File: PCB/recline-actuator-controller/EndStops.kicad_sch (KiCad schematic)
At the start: 0 parts

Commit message: Recline Actuator Control
Recline controller board schematic and Recline actuator board schematics. Actuator control board schematic 90% complete.
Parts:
- added J12, J13, J14, J15: 0705530002, AVR-KiCAD-Lib-Connectors:Pin_Header_Angled_1x03_Pitch2.54mm, symbol AVR-KiCAD-Lib-Connectors:0705530002
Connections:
- new net +3.3V: J12.3, J13.3, J14.3, J15.3
- new net GND: J12.2, J13.2, J14.2, J15.2
- new net MAX1: J12.1
- new net MAX2: J14.1
- new net MIN1: J13.1
- new net MIN2: J15.1
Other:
- note added: "Endstops"

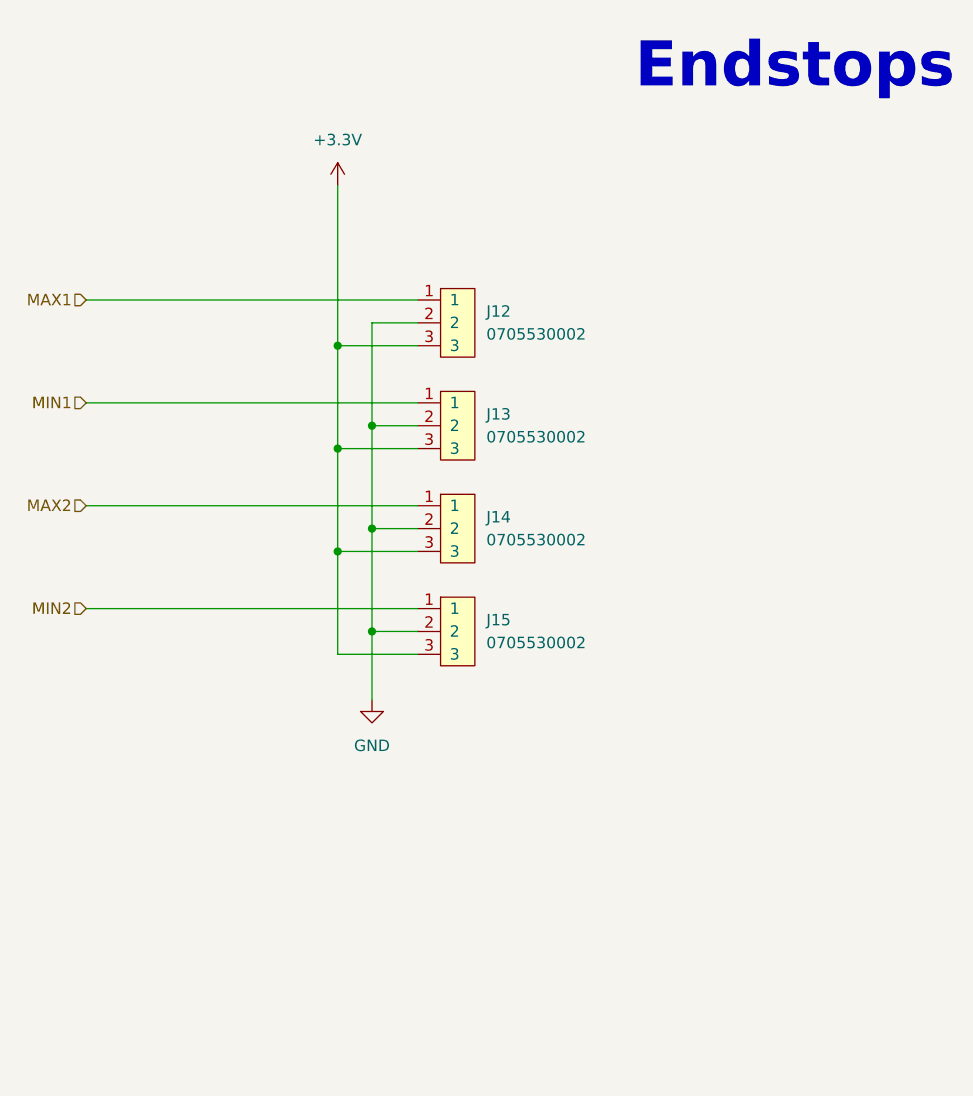
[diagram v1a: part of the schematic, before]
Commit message: Actuator Control Schematic
Schematic for Actuator control board completed! Once reviewed PCB layout will start.
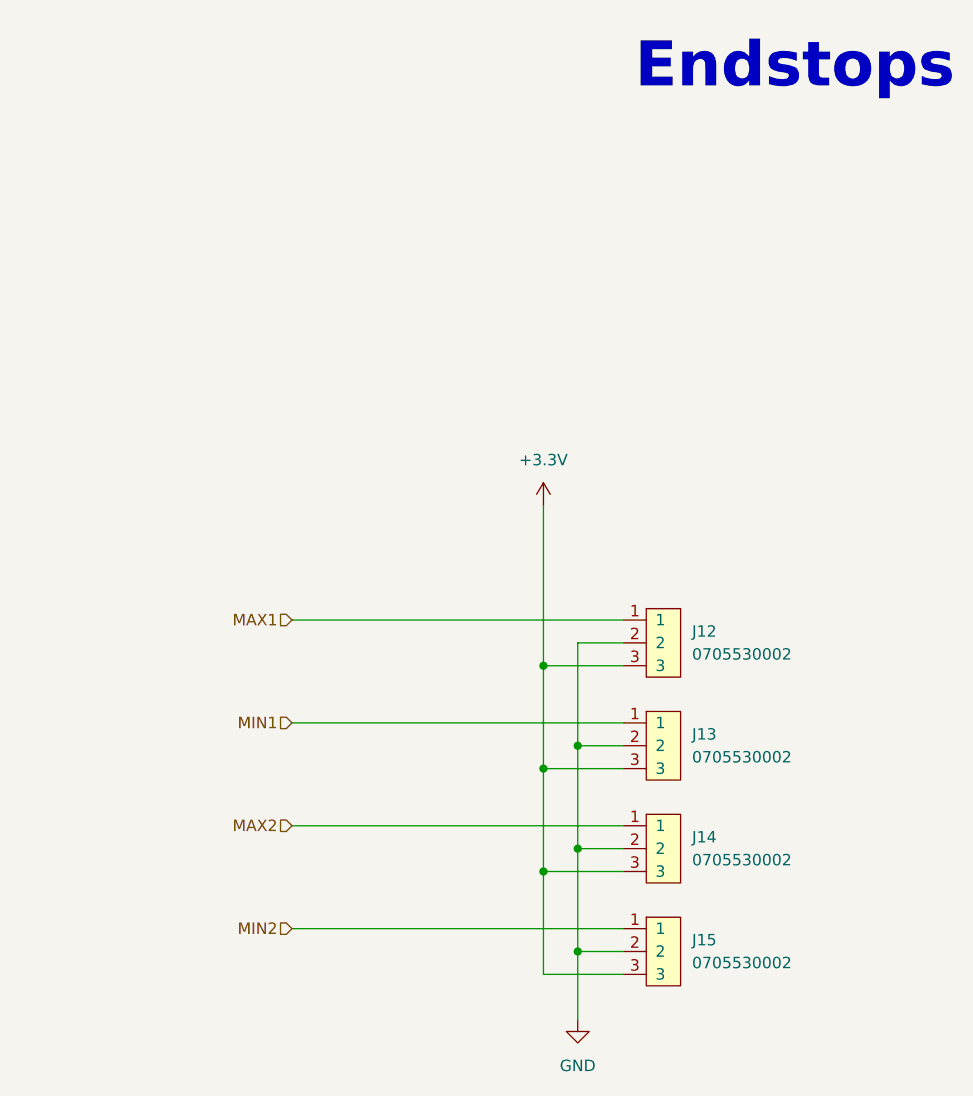
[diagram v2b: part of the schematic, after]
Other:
- moved on the sheet: J12, J13, J14, J15

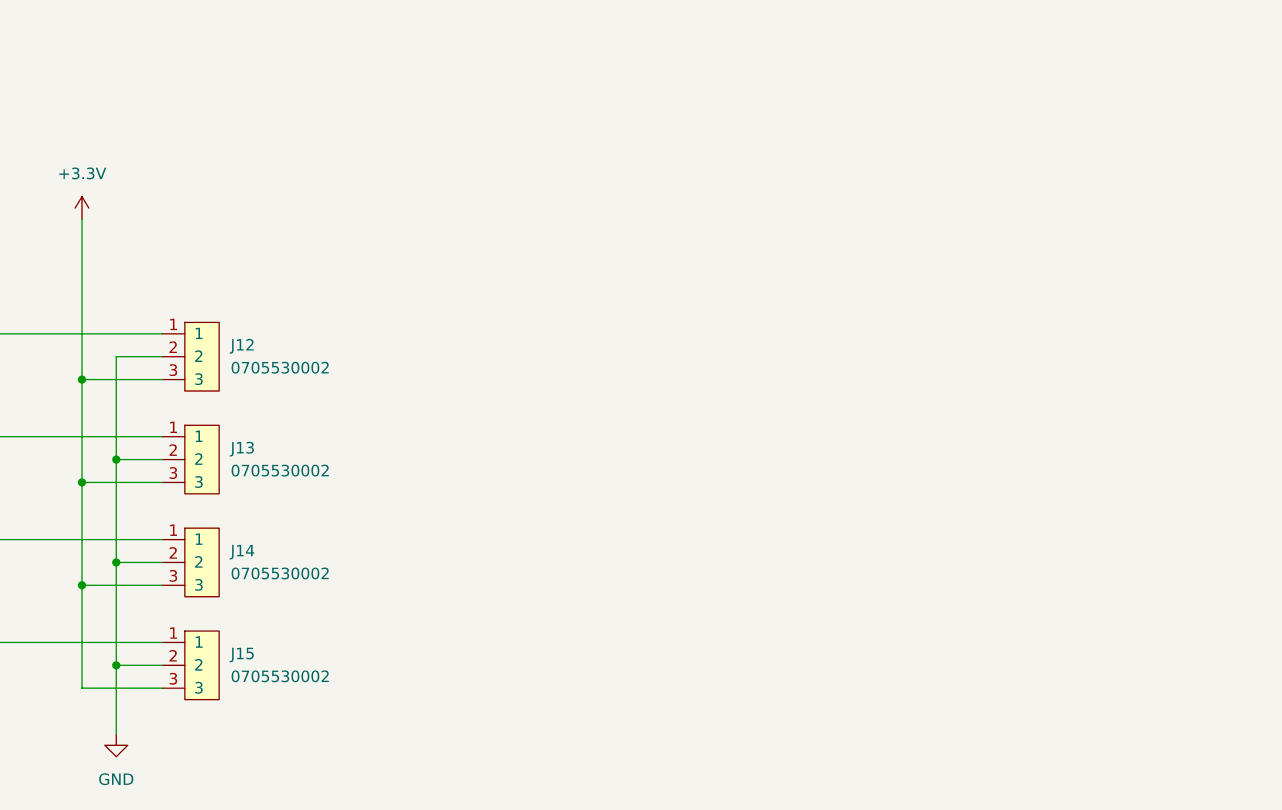
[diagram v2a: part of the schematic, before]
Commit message: More Motor Channels
Adding more motor channels to actuator control board it will need new MCU or port expansion.
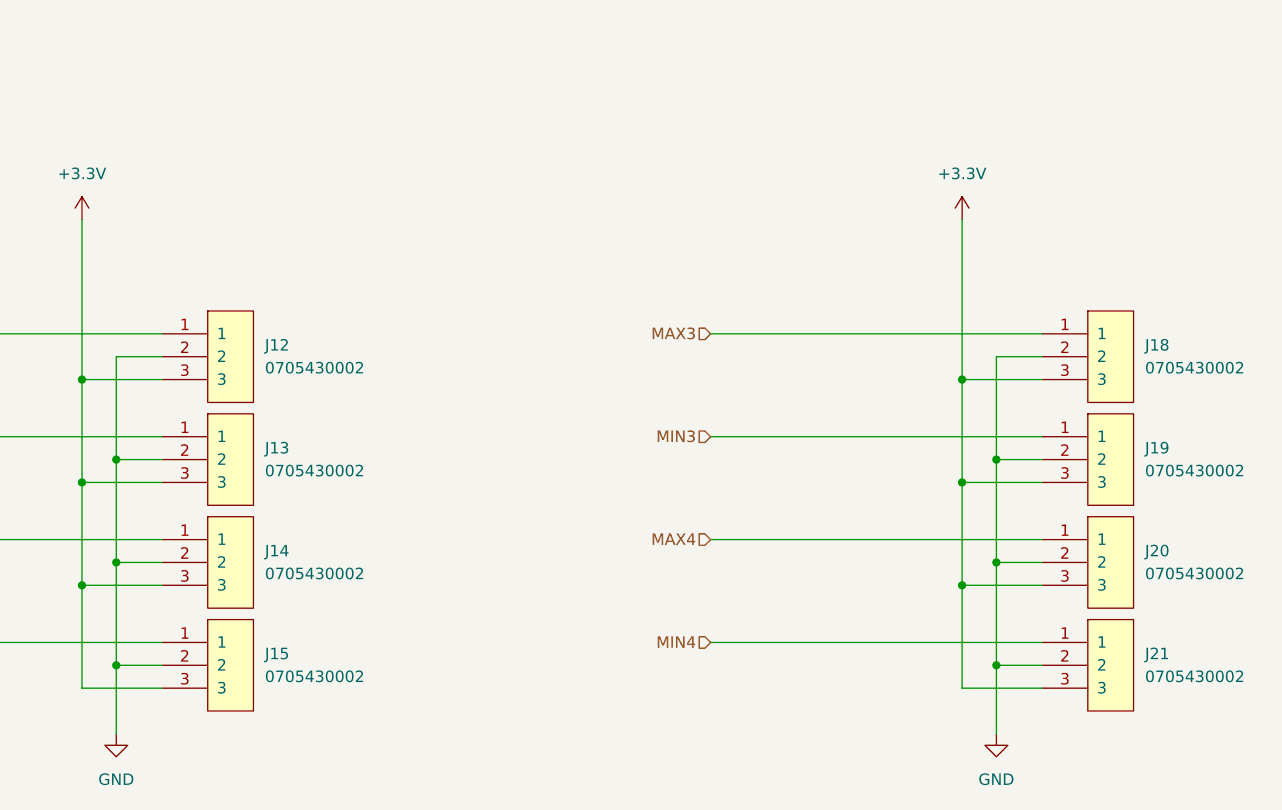
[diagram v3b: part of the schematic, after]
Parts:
- removed J12, J13, J14, J15: 0705530002, AVR-KiCAD-Lib-Connectors:Pin_Header_Angled_1x03_Pitch2.54mm, symbol AVR-KiCAD-Lib-Connectors:0705530002
- added J12, J13, J14, J15, J18, J19, J20, J21: 0705430002, AVR-KiCAD-Lib-Connectors:Shrouded_Pin_Header_Straight_1x03_Pitch2.54mm, symbol AVR-KiCAD-Lib-Connectors:0705430002
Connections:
- net +3.3V: now also J12.3, J13.3, J14.3, J15.3, J18.3, J19.3, J20.3, J21.3
- net GND: now also J12.2, J13.2, J14.2, J15.2, J18.2, J19.2, J20.2, J21.2
- net MAX1: now also J12.1
- net MAX2: now also J14.1
- net MIN1: now also J13.1
- net MIN2: now also J15.1
- new net MAX3: J18.1
- new net MAX4: J20.1
- new net MIN3: J19.1
- new net MIN4: J21.1

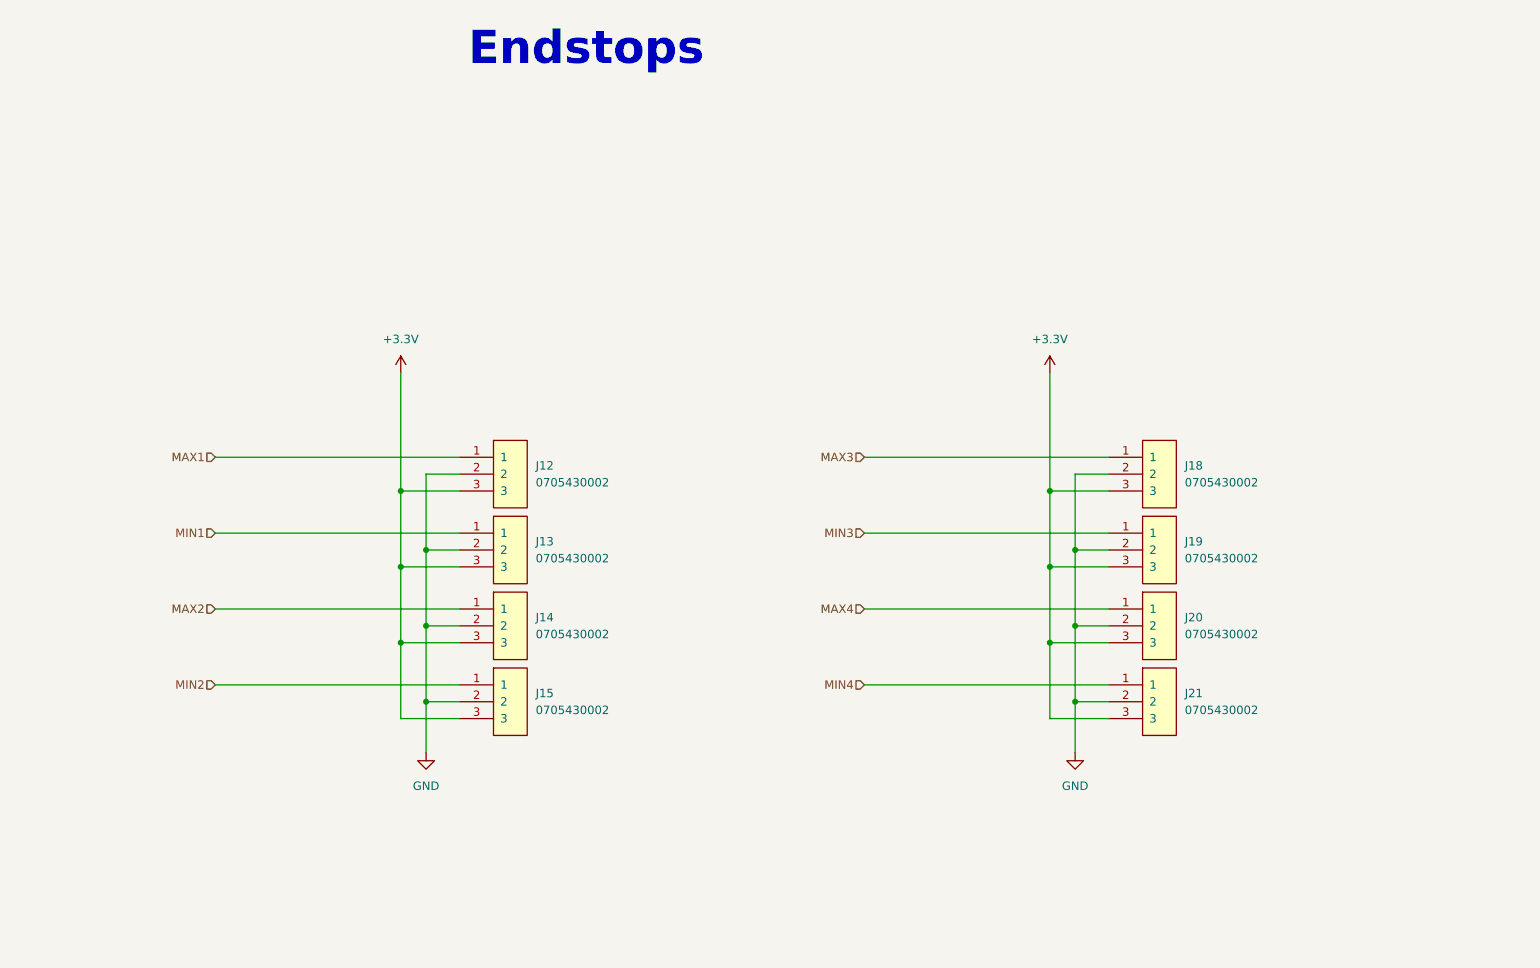
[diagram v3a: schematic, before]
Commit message: Recline Actuator Board Redesign
Recline actuator control board redesign complete, functionality extended to handle two additional large actuators for leg lifting. Air compressor switching circuit made to handle higher current. Additional end stops for additional actuators added, IO expander added for more input to RP2040. Current sensing for all 4 actuators.
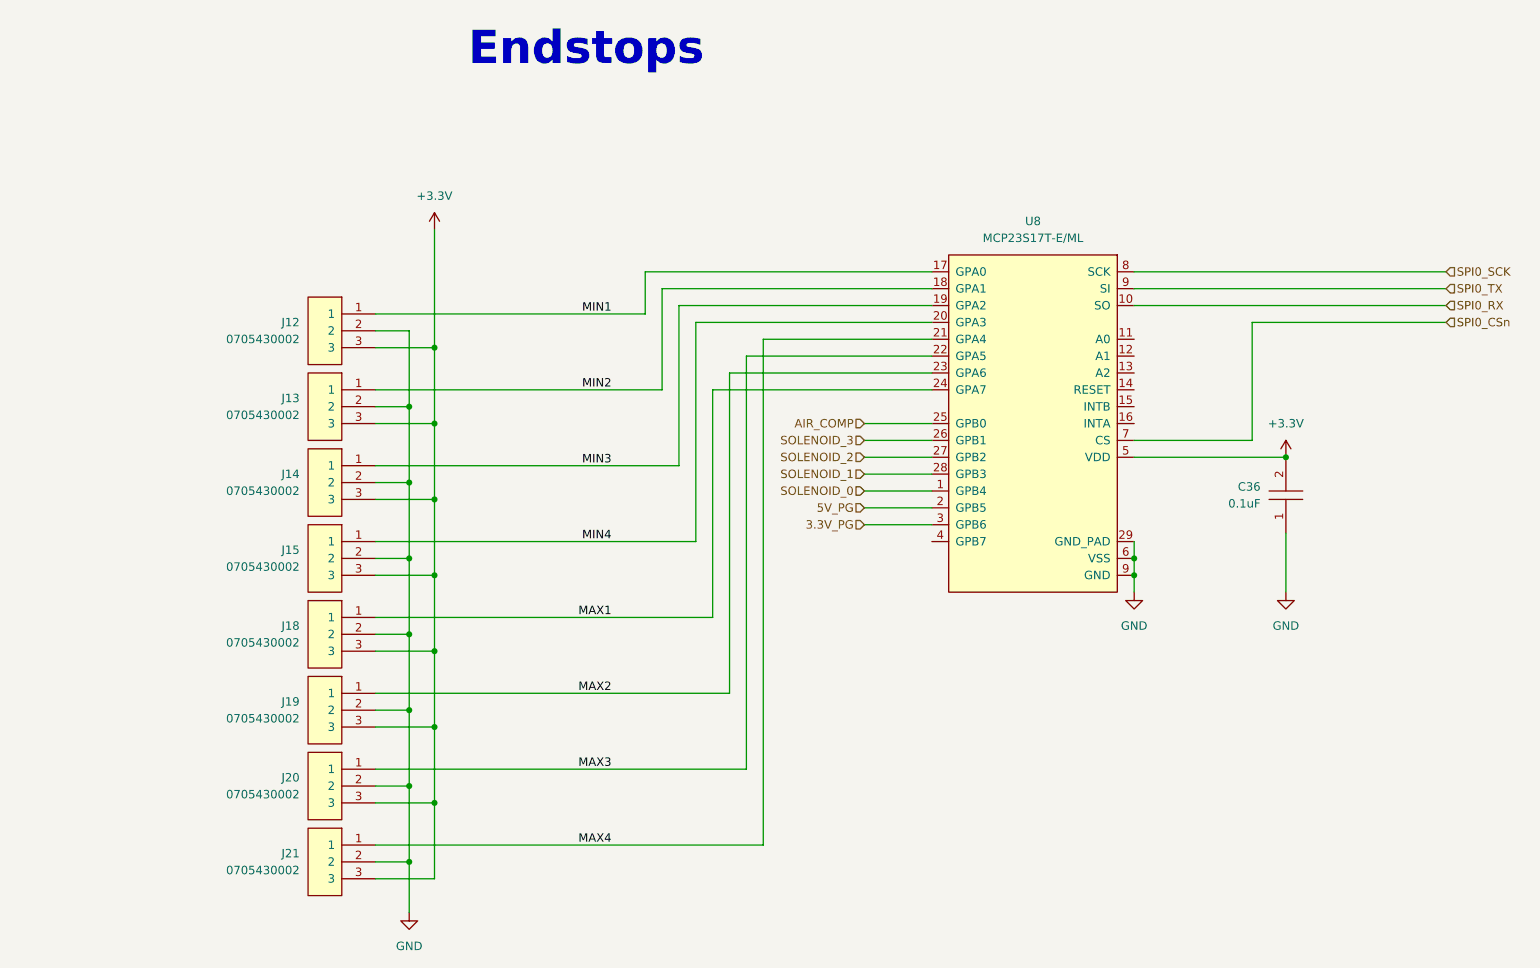
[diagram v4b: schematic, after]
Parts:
- added C36: C0402C104K9PACTU, AVR-KiCAD-Lib-Resistors:R0402, symbol AVR-KiCAD-Lib-Capacitors:C0402C104K9PACTU
- added U8: MCP23S17T-E/ML, AVR-KiCAD-Lib-ICs:QFN28_6x6MC_MCH-L, symbol AVR-KiCAD-Lib-ICs:MCP23S17T-E/ML
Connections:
- net +3.3V: now also C36.2, U8.5 (VDD)
- net GND: now also C36.1, U8.29 (GND_PAD), U8.6 (VSS), U8.9 (SI)
- net MAX1: now also J18.1, U8.24 (GPA7); no longer J12.1
- net MAX2: now also J19.1, U8.23 (GPA6); no longer J14.1
- net MAX3: now also J20.1, U8.22 (GPA5); no longer J18.1
- net MAX4: now also J21.1, U8.21 (GPA4); no longer J20.1
- net MIN1: now also J12.1, U8.17 (GPA0); no longer J13.1
- net MIN2: now also J13.1, U8.18 (GPA1); no longer J15.1
- net MIN3: now also J14.1, U8.19 (GPA2); no longer J19.1
- net MIN4: now also J15.1, U8.20 (GPA3); no longer J21.1
- new net 3.3V_PG: U8.3 (GPB6)
- new net 5V_PG: U8.2 (GPB5)
- new net AIR_COMP: U8.25 (GPB0)
- new net SOLENOID_0: U8.1 (GPB4)
- new net SOLENOID_1: U8.28 (GPB3)
- new net SOLENOID_2: U8.27 (GPB2)
- new net SOLENOID_3: U8.26 (GPB1)
- new net SPI0_CSn: U8.7 (CS)
- new net SPI0_RX: U8.10 (SO)
- new net SPI0_SCK: U8.8 (SCK)
- new net SPI0_TX: U8.9 (SI)
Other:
- moved on the sheet: J12, J13, J14, J15, J18, J19, J20, J21

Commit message: Via Stichign and Pullups
Added optional pullups to endstop circuit.  Revised via stitching for input power, revised layout with added via stitching and copper pours for solenoid mosfets.
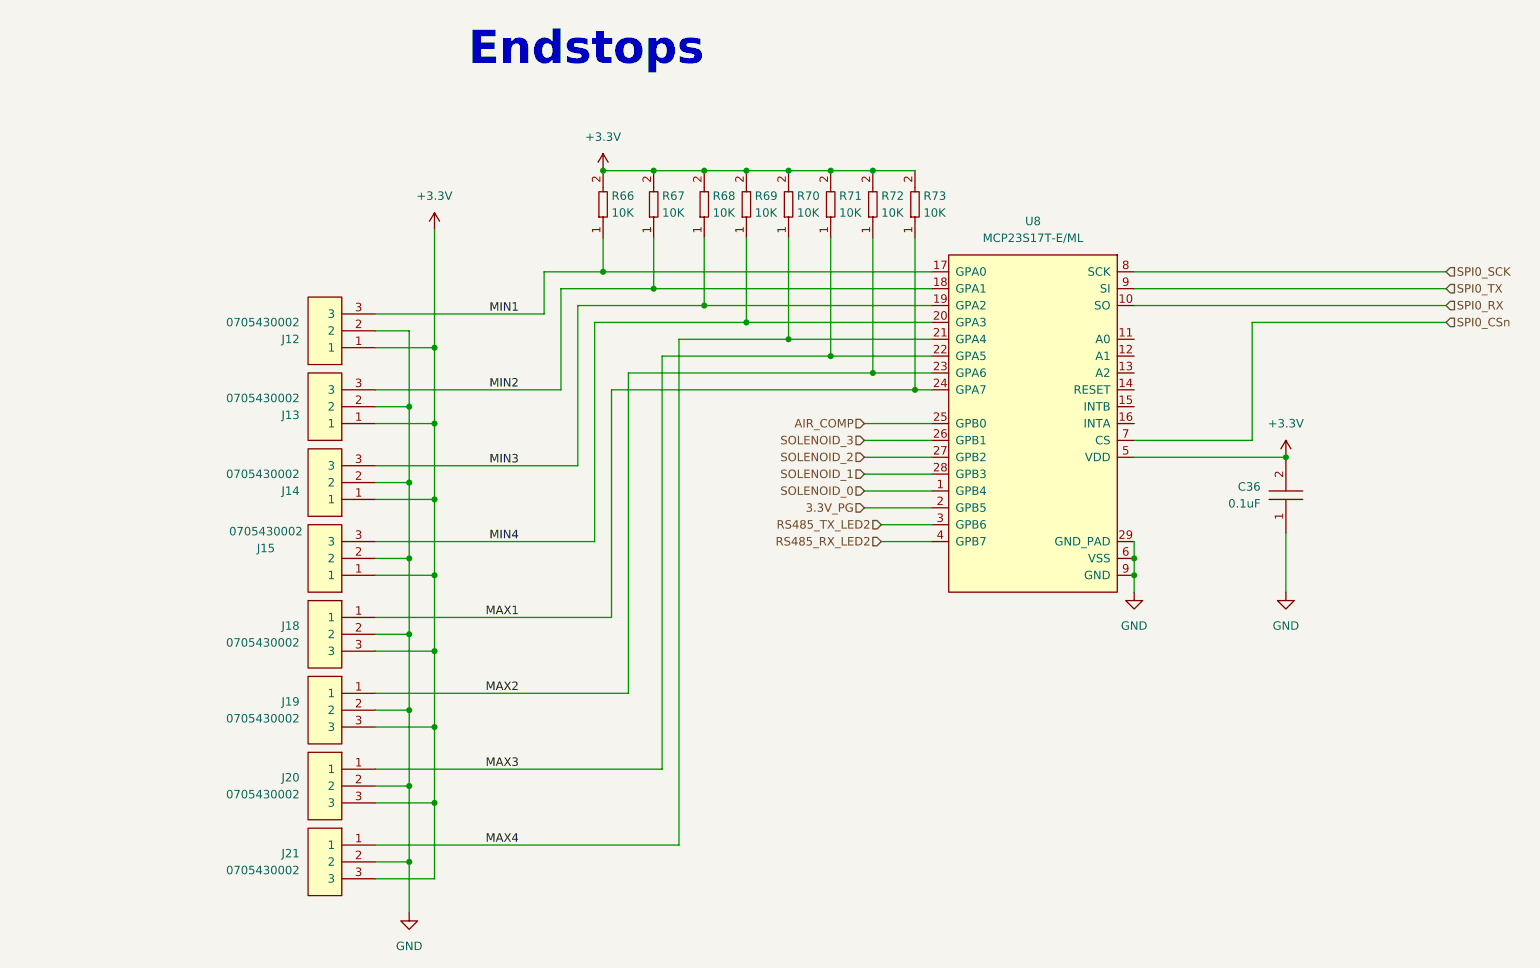
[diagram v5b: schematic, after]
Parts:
- added R66, R67, R68, R69, R70, R71, R72, R73: RC0402FR-0710KL, AVR-KiCAD-Lib-Resistors:R0402, symbol AVR-KiCAD-Lib-Resistors:RC0402FR-0710KL
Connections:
- net 5V_PG is gone; now on net 3.3V_PG: U8.2 (GPB5)
- net +3.3V: now also J12.1, J13.1, J14.1, J15.1, R66.2, R67.2, R68.2, R69.2, R70.2, R71.2, R72.2, R73.2; no longer J12.3, J13.3, J14.3, J15.3
- net 3.3V_PG: no longer U8.3 (GPB6)
- net MAX1: now also R73.1
- net MAX2: now also R72.1
- net MAX3: now also R71.1
- net MAX4: now also R70.1
- net MIN1: now also J12.3, R66.1; no longer J12.1
- net MIN2: now also J13.3, R67.1; no longer J13.1
- net MIN3: now also J14.3, R68.1; no longer J14.1
- net MIN4: now also J15.3, R69.1; no longer J15.1
- net RS485_RX_LED2: now reaches U8.4 (GPB7)
- new net RS485_TX_LED2: U8.3 (GPB6)
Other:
- moved on the sheet: J12, J13, J14, J15
